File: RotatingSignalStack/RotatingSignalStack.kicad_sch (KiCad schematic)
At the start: 23 parts, among them IC1 STM32H562RIT6, J1 RJ45_LED_Shielded, U2 DP83825I

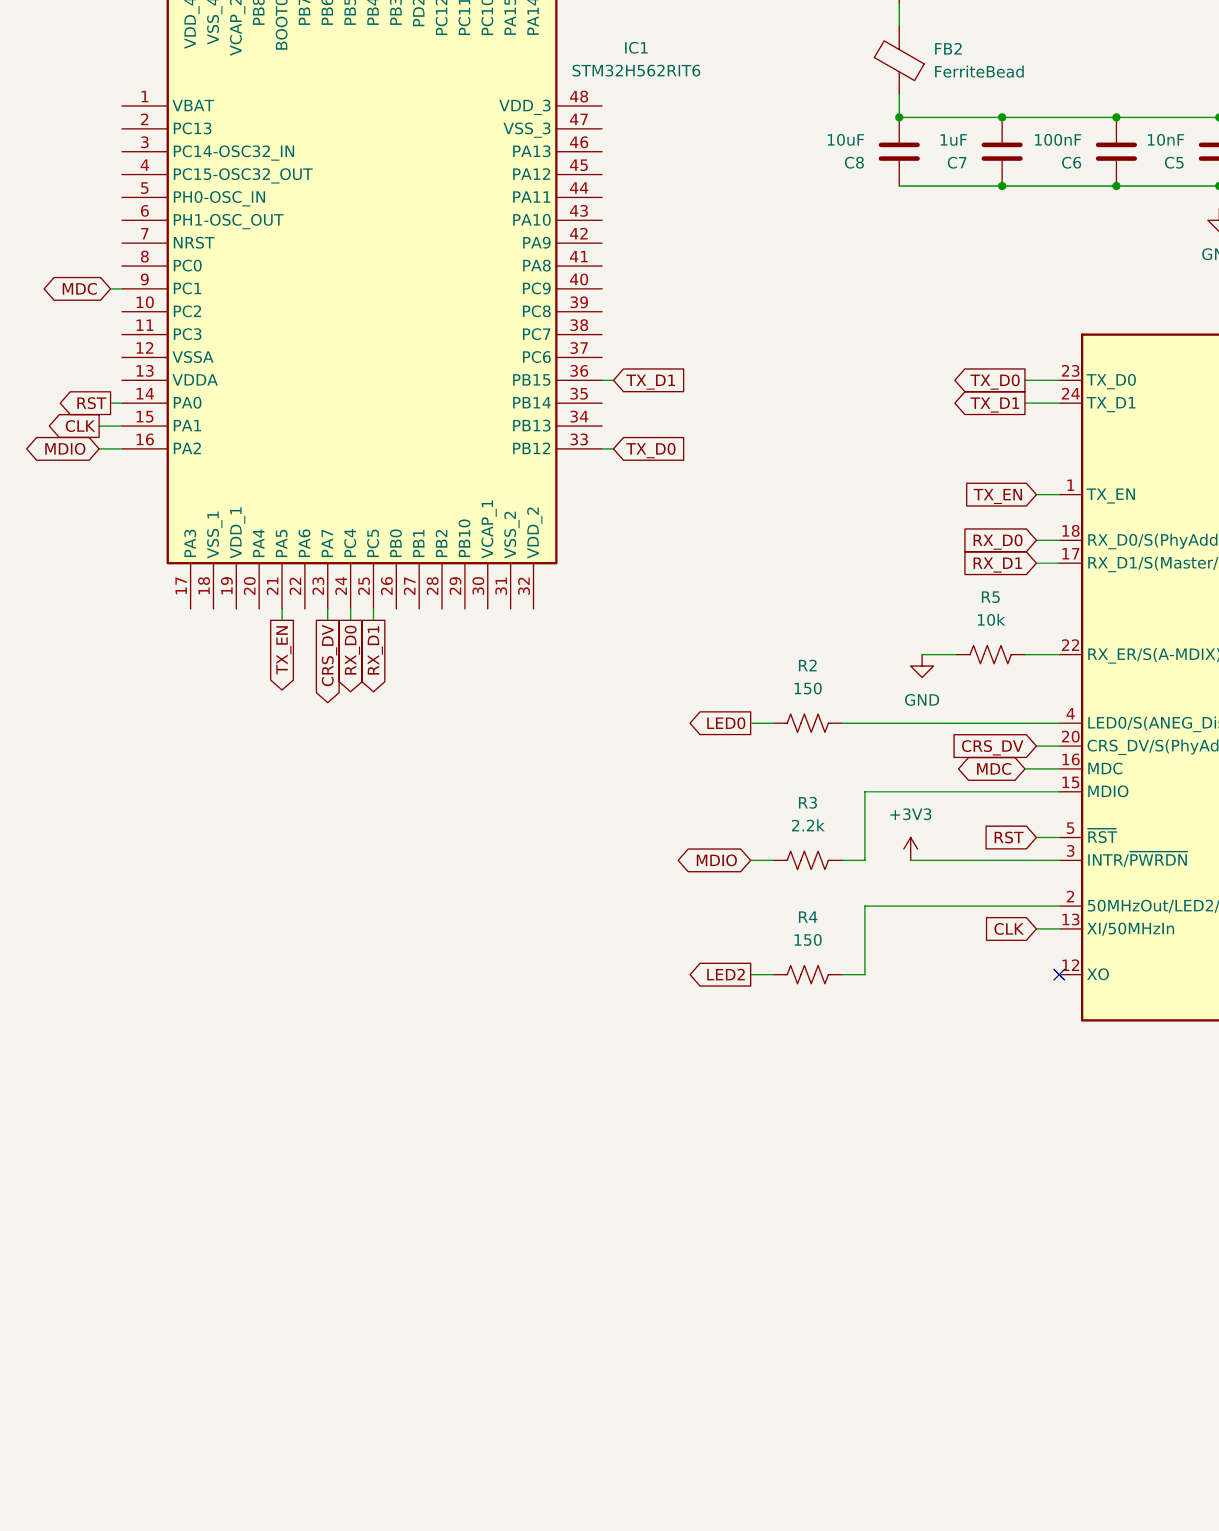
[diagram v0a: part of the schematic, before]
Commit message: Added CAN Transceiver and Power Converter
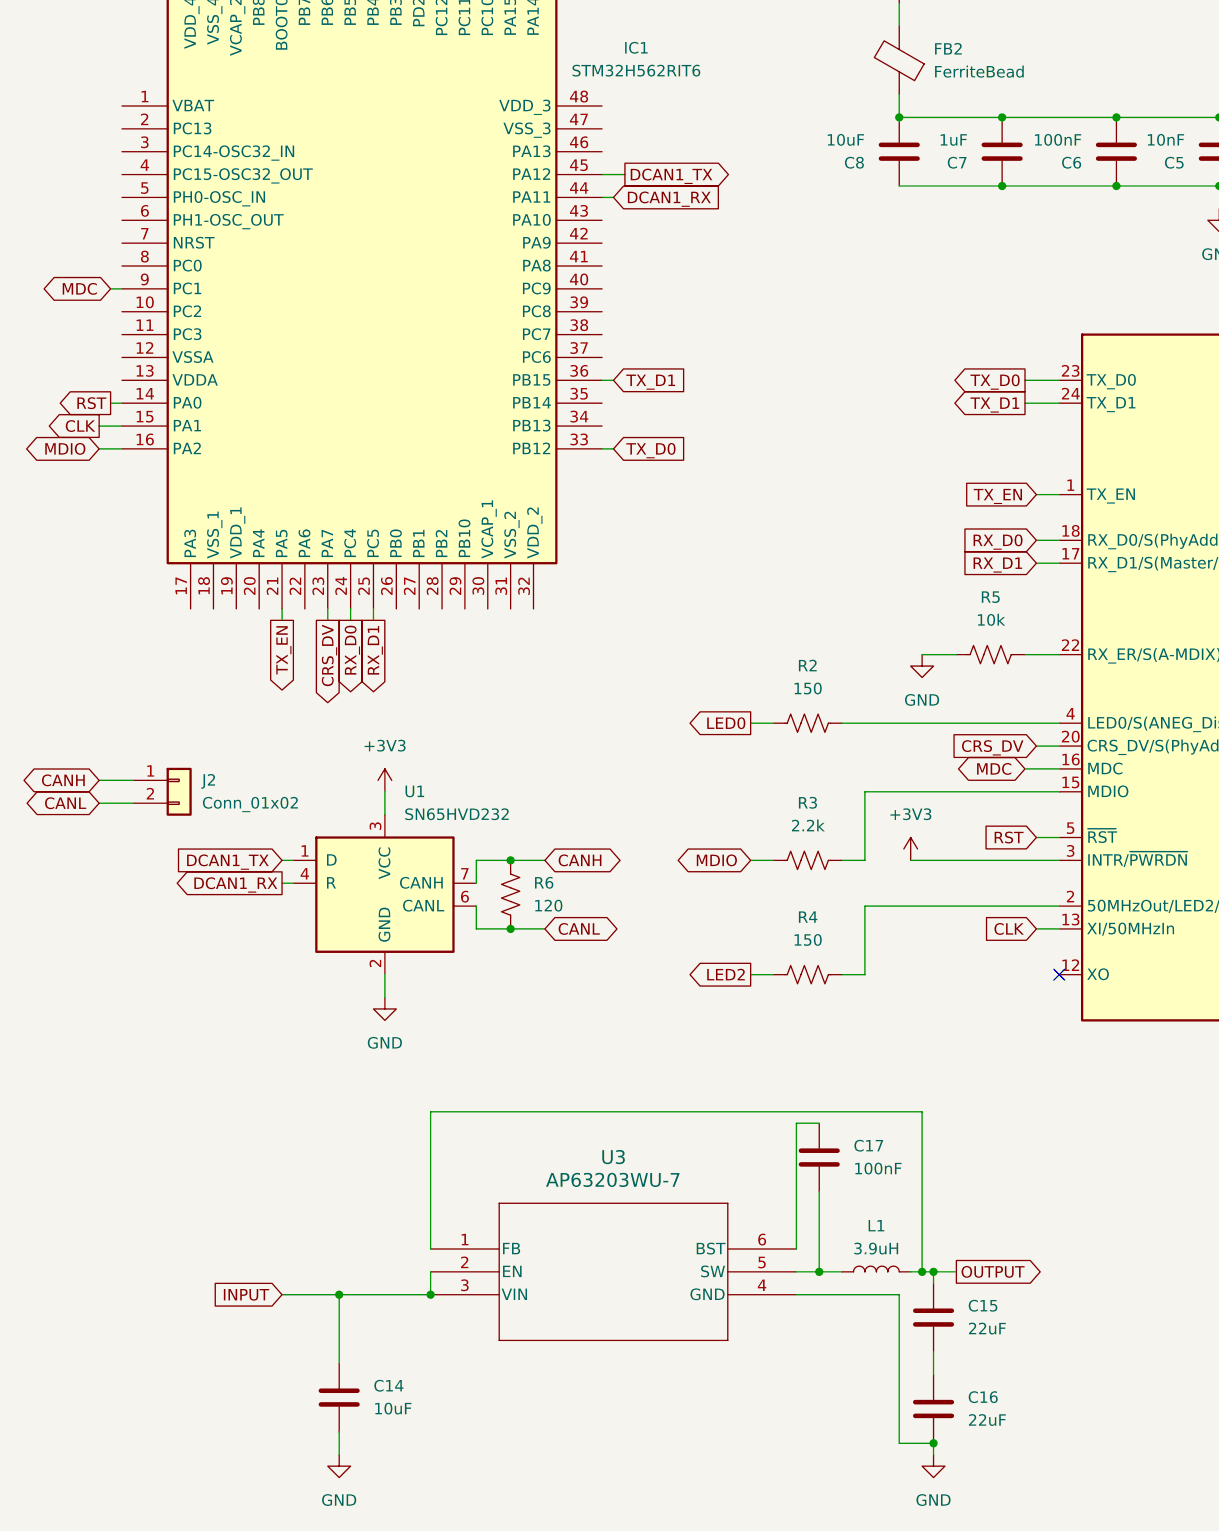
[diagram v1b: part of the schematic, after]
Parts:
- added C14: 10uF, symbol Device:C
- added C15, C16: 22uF, symbol Device:C
- added C17: 100nF, symbol Device:C
- added J2: Conn_01x02, Connector_JST:JST_SH_SM02B-SRSS-TB_1x02-1MP_P1.00mm_Horizontal, symbol Connector_Generic:Conn_01x02
- added L1: 3.9uH, symbol Device:L
- added R6: 120, symbol Device:R_US
- added U1: SN65HVD232, Package_SO:SOIC-8_3.9x4.9mm_P1.27mm, symbol Interface_CAN_LIN:SN65HVD232
- added U3: AP63203WU-7, AP63203WU-7_DIO, symbol AP63203WU-7:AP63203WU-7
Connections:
- net +3V3: now also U1.3 (VCC)
- net GND: now also C14.2, C16.2, U1.2 (GND), U3.4 (GND)
- net DCAN1_RX: now reaches IC1.44 (PA11)
- net DCAN1_RX: now also U1.4 (R)
- net DCAN1_TX: now reaches IC1.45 (PA12)
- net DCAN1_TX: now also U1.1 (D)
- new net: C15.2, C16.1
- new net: C17.2, L1.1, U3.5 (SW)
- new net: C17.1, U3.6 (BST)
- new net CANH: J2.1 (Pin_1), R6.1, U1.7 (CANH)
- new net CANL: J2.2 (Pin_2), R6.2, U1.6 (CANL)
- new net INPUT: C14.1, U3.2 (EN), U3.3 (VIN)
- new net OUTPUT: C15.1, L1.2, U3.1 (FB)

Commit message: POE Progress
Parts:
- removed C13: 0.1uF, symbol Device:C_Small
- removed J1: RJ45_LED_Shielded, symbol Connector:RJ45_LED_Shielded
- added C18: 0.01µF (cermanic), symbol Device:C
- added R7, R8: 1k, symbol Device:R_US
- added U4: TMAG5273C1QDBVR, TMAG5273C1QDBVR:SOT95P280X140-6N, symbol TMAG5273C1QDBVR:TMAG5273C1QDBVR
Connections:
- net +3V3: now also C18.1, R7.1, R8.1, U4.4 (VCC)
- net GND: now also C18.2, U4.2 (GND), U4.3 (TEST), U4.5 (~{INT})
- net I2C3_SDA: now reaches IC1.40 (PC9)
- net I2C3_SDA: now also R8.2, U4.6 (SDA)
- net I2C3_SCL: now reaches IC1.41 (PA8)
- net I2C3_SCL: now also R7.2, U4.1 (SCL)
- no-connect marks 2 -> 1
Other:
- added sheet Ethernet (ethernet.kicad_sch)
- moved on the sheet: C14, C15, C16, C17, L1, U3

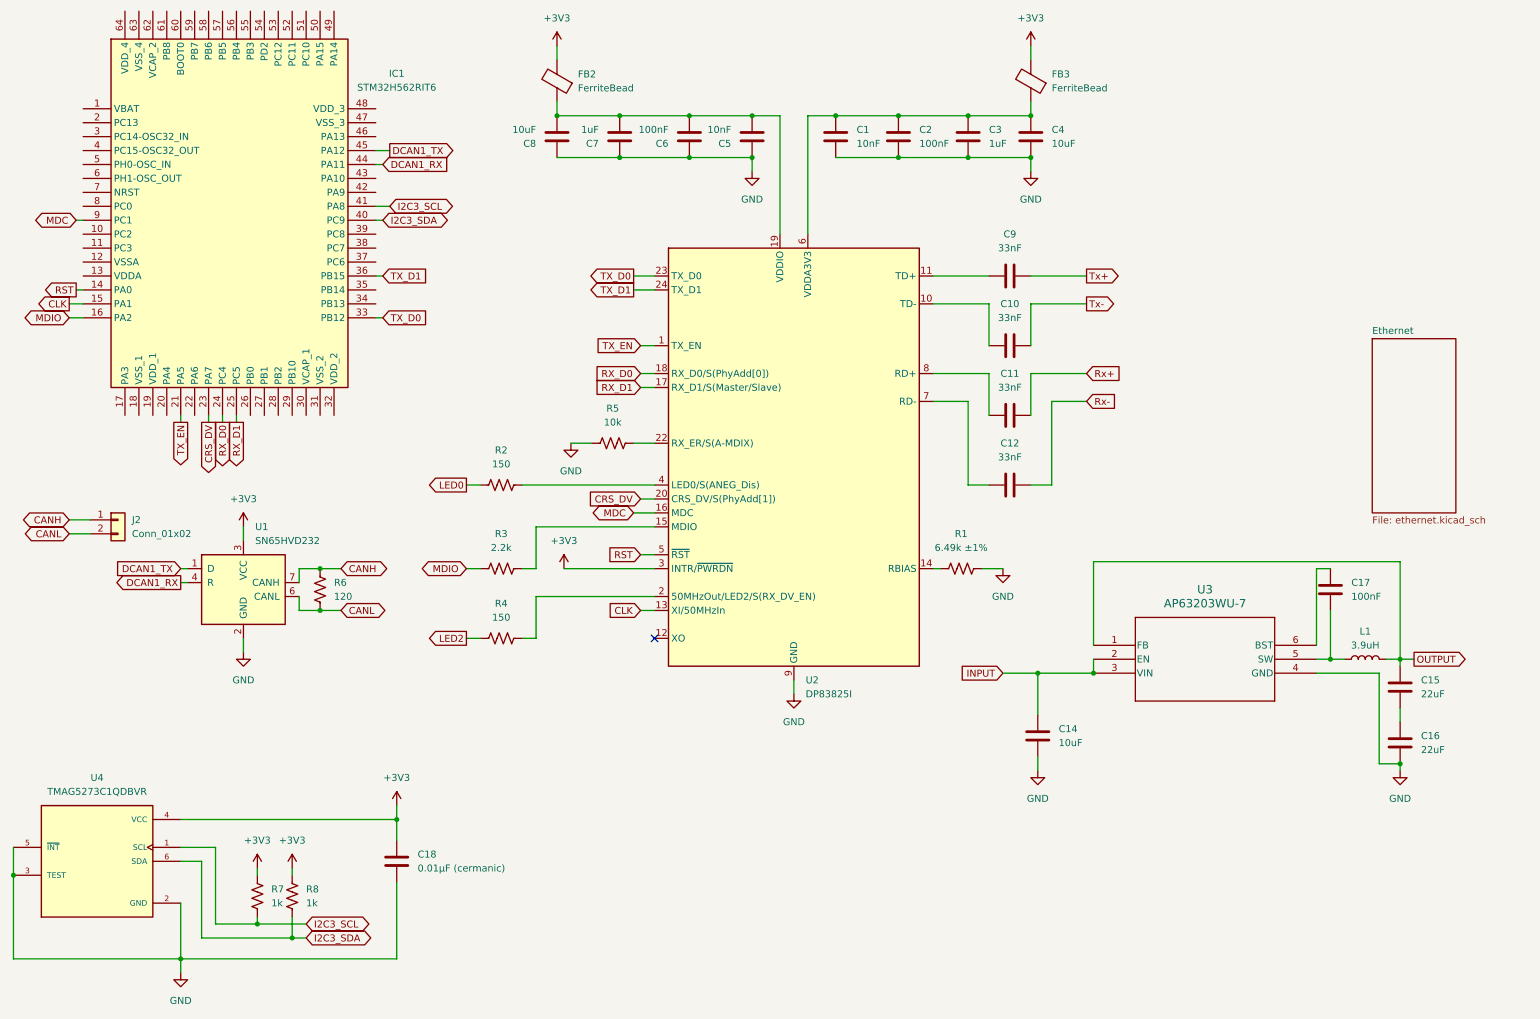
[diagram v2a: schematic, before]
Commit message: Added ethernet magnetics
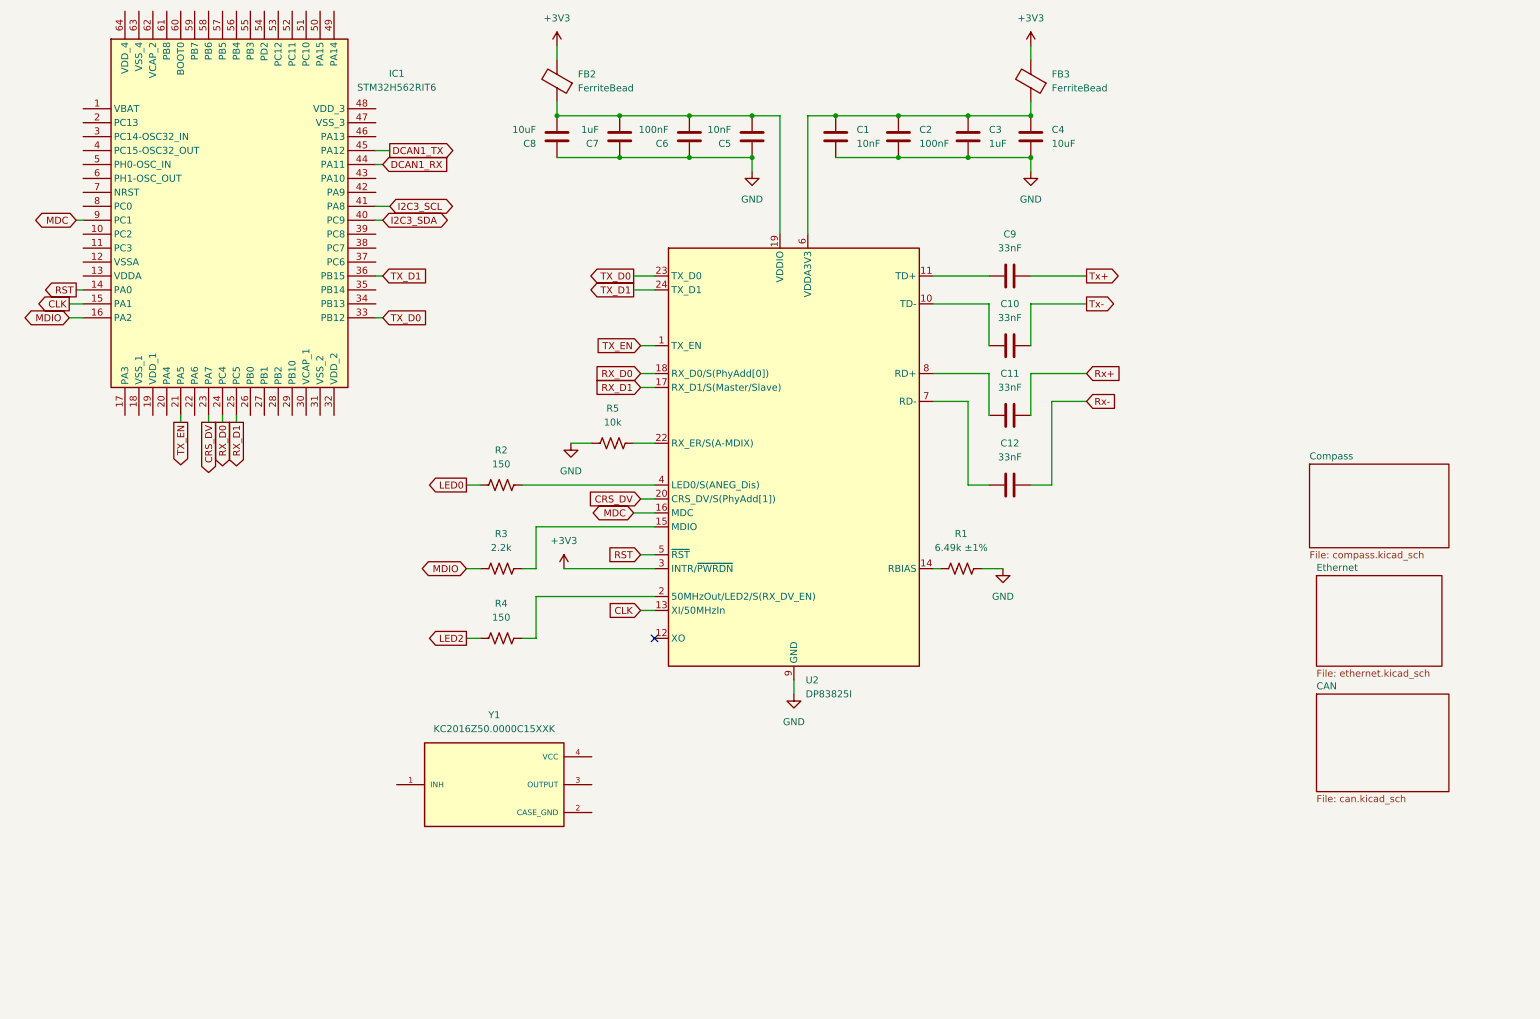
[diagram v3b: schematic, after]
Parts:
- removed C14: 10uF, symbol Device:C
- removed C15, C16: 22uF, symbol Device:C
- removed C17: 100nF, symbol Device:C
- removed C18: 0.01µF (cermanic), symbol Device:C
- removed J2: Conn_01x02, Connector_JST:JST_SH_SM02B-SRSS-TB_1x02-1MP_P1.00mm_Horizontal, symbol Connector_Generic:Conn_01x02
- removed L1: 3.9uH, symbol Device:L
- removed R6: 120, symbol Device:R_US
- removed R7, R8: 1k, symbol Device:R_US
- removed U1: SN65HVD232, Package_SO:SOIC-8_3.9x4.9mm_P1.27mm, symbol Interface_CAN_LIN:SN65HVD232
- removed U3: AP63203WU-7, AP63203WU-7_DIO, symbol AP63203WU-7:AP63203WU-7
- removed U4: TMAG5273C1QDBVR, TMAG5273C1QDBVR:SOT95P280X140-6N, symbol TMAG5273C1QDBVR:TMAG5273C1QDBVR
- added Y1: KC2016Z50.0000C15XXK, KC2016Z50.0000C15XXK:OSC_KC2016Z50.0000C15XXK-4, symbol KC2016Z50.0000C15XXK:KC2016Z50.0000C15XXK
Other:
- added sheet CAN (can.kicad_sch)
- added sheet Compass (compass.kicad_sch)

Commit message: Added Oscillator, New Magnetics, Sheet Pins
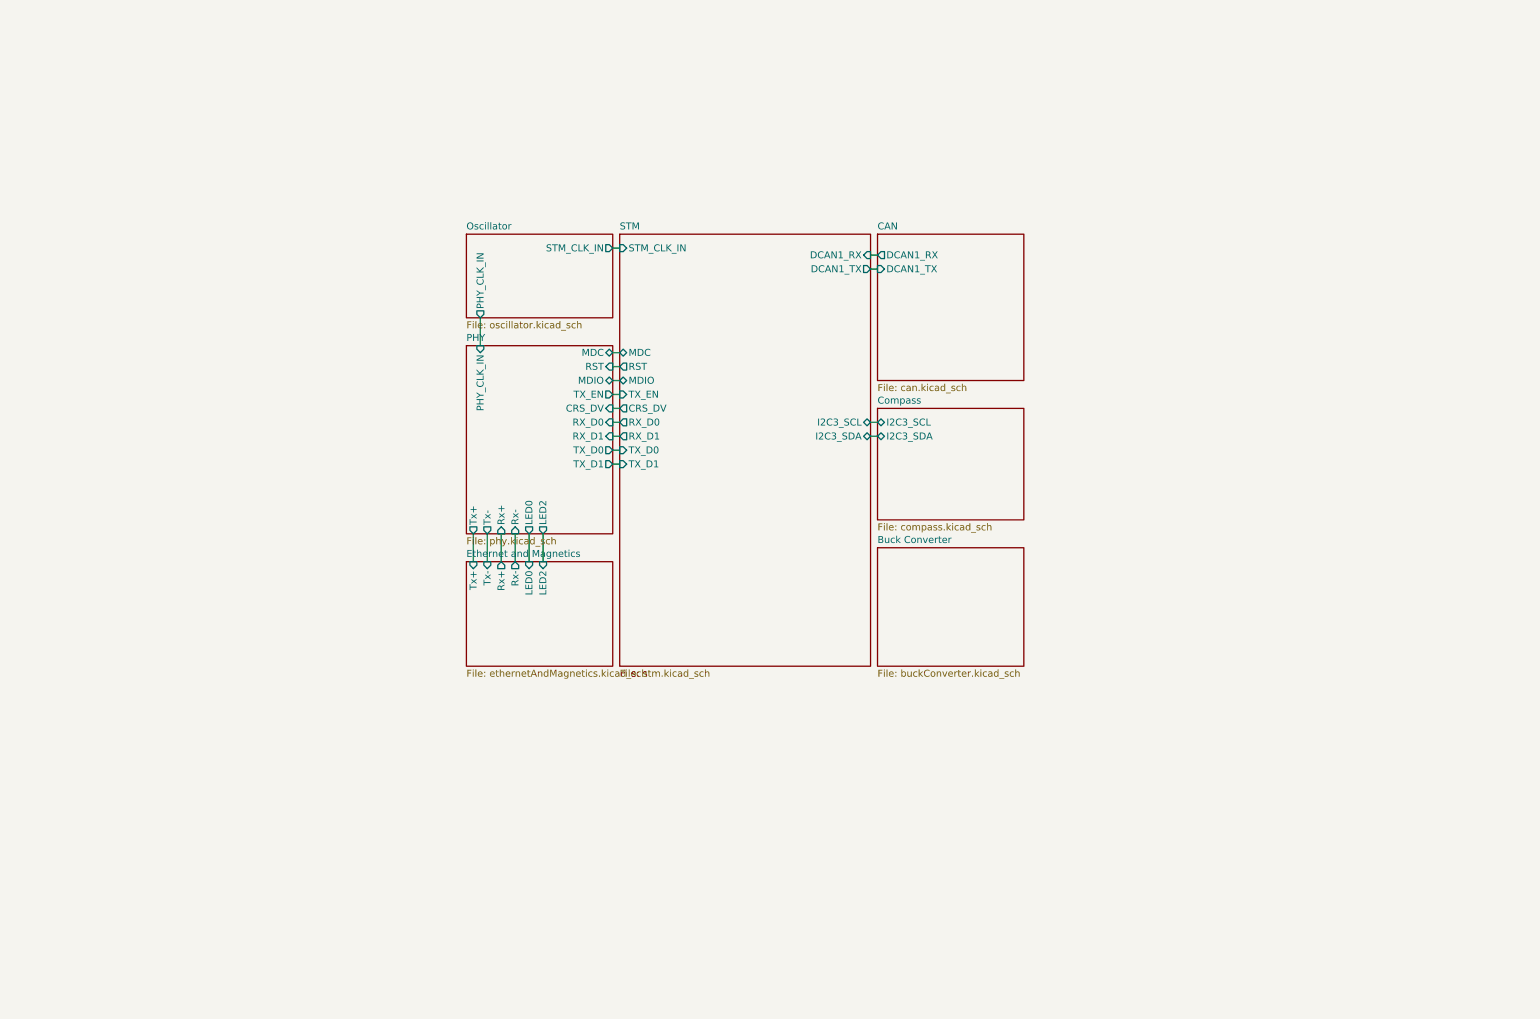
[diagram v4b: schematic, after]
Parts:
- removed C1, C5: 10nF, symbol Device:C
- removed C10, C11, C12, C9: 33nF, symbol Device:C
- removed C2, C6: 100nF, symbol Device:C
- removed C3, C7: 1uF, symbol Device:C
- removed C4, C8: 10uF, symbol Device:C
- removed FB2, FB3: FerriteBead, symbol Device:FerriteBead
- removed IC1: STM32H562RIT6, QFP50P1200X1200X160-64N, symbol STM32H562RIT6:STM32H562RIT6
- removed R1: 6.49k ±1%, symbol Device:R_US
- removed R2, R4: 150, symbol Device:R_US
- removed R3: 2.2k, symbol Device:R_US
- removed R5: 10k, symbol Device:R_US
- removed U2: DP83825I, Package_DFN_QFN:Texas_RMQ0024A_WQFN-24-1EP_3x3mm_P0.4mm_EP1.9x1.9mm, symbol Interface_Ethernet:DP83825I
- removed Y1: KC2016Z50.0000C15XXK, KC2016Z50.0000C15XXK:OSC_KC2016Z50.0000C15XXK-4, symbol KC2016Z50.0000C15XXK:KC2016Z50.0000C15XXK
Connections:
- no-connect marks 1 -> 0
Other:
- sheet Ethernet renamed Ethernet and Magnetics
- added sheet Buck Converter (buckConverter.kicad_sch)
- added sheet Oscillator (oscillator.kicad_sch)
- added sheet PHY (phy.kicad_sch)
- added sheet STM (stm.kicad_sch)
- sheet CAN ports: added DCAN1_RX, DCAN1_TX; removed none
- sheet Compass ports: added I2C3_SCL, I2C3_SDA; removed none
- sheet Ethernet and Magnetics: file ethernet.kicad_sch -> ethernetAndMagnetics.kicad_sch
- sheet Ethernet and Magnetics ports: added LED0, LED2, Rx+, Rx-, Tx+, Tx-; removed none
